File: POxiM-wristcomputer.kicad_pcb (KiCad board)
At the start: 4 copper layers, 40 x 27 mm, 91 parts, among them J1 USB_B_Micro, J14 Jumper_NO_Small, J2 AudioJack4_Ground

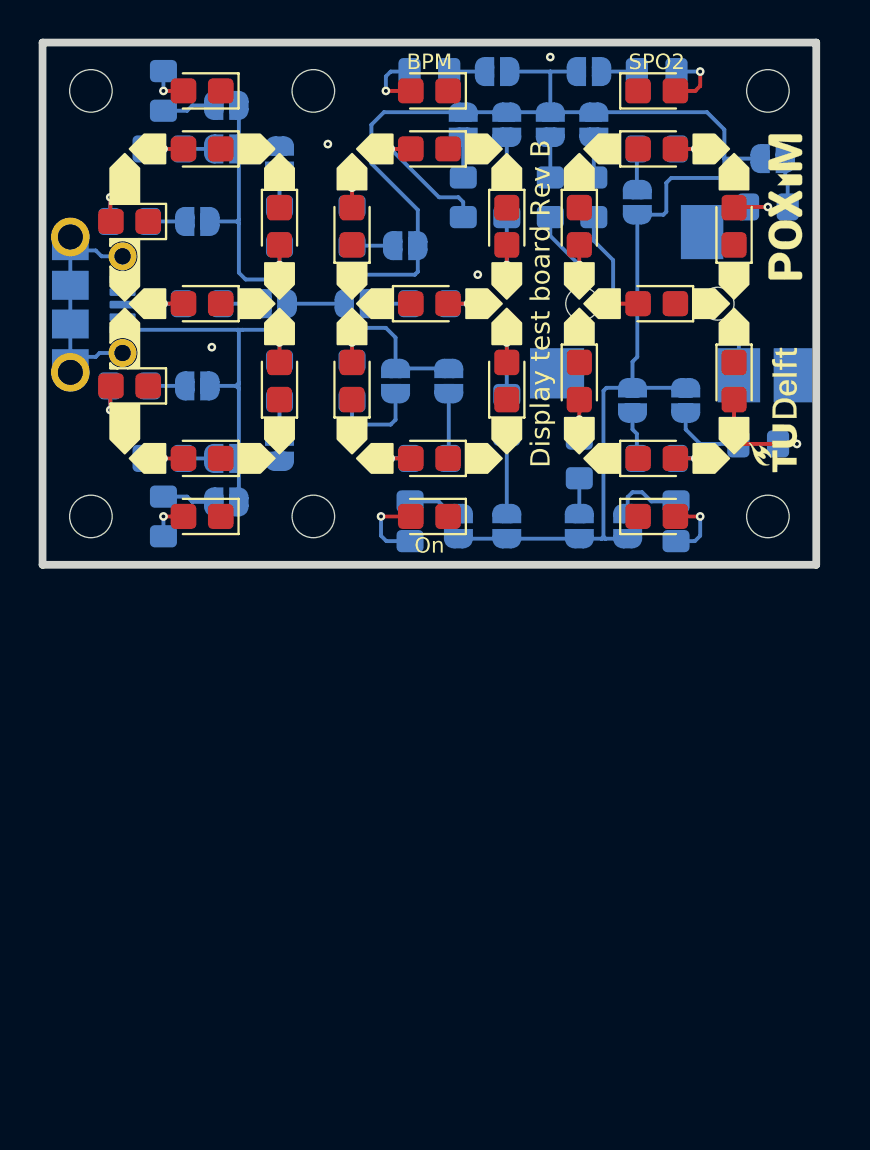
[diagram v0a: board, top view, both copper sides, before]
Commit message: Start reworking sing supply ripple issues.
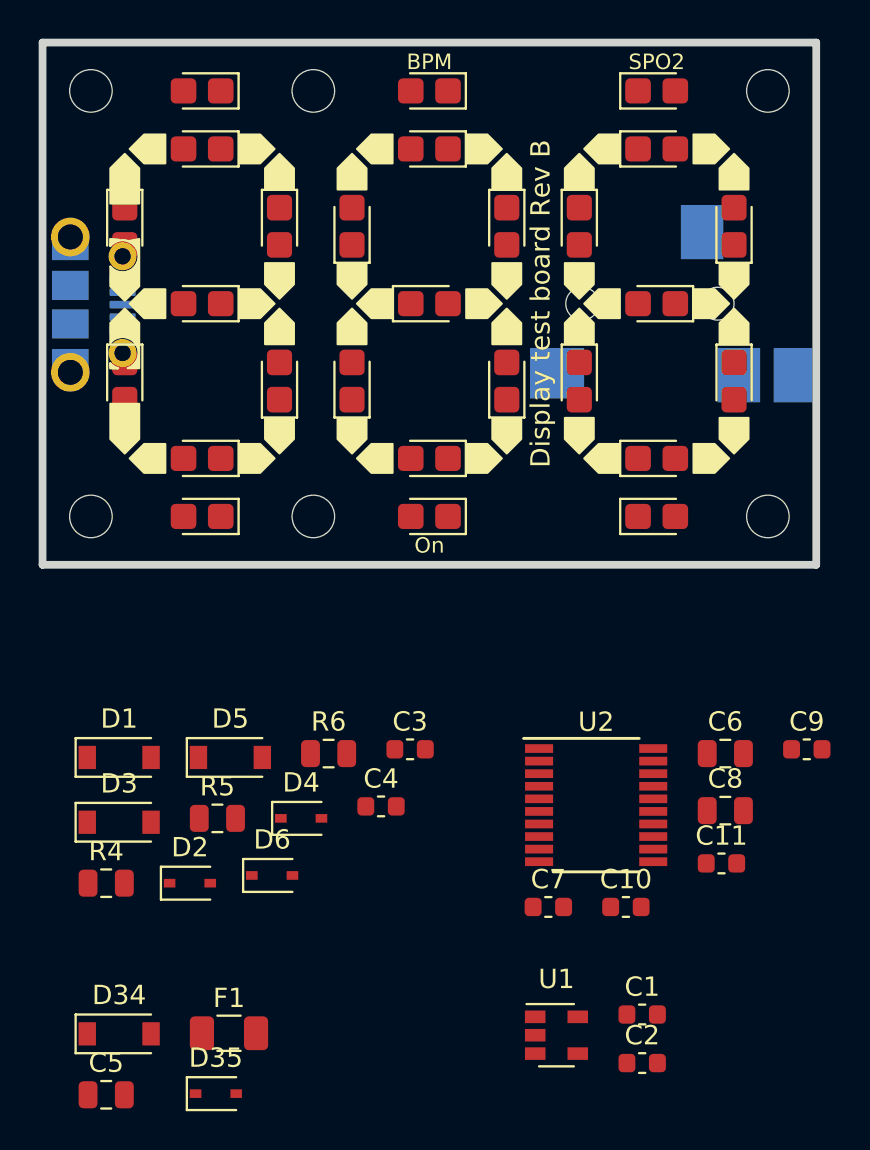
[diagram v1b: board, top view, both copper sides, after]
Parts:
- removed the D10 at (82.2, 127.5)
- removed the D23 at (94.0, 127.5)
- removed the D25 at (94.0, 135.5)
- removed the D28 at (86.0, 135.5)
- removed the D29 at (86.0, 127.5)
- removed G***: LOGO, POxiM-logos:TUDelftLogo_W7_5mm
- removed G***: LOGO, POxiM-logos:POxiMLogo_GoldHeart_W7_5mm
- removed J14, JP1, JP16, JP18, JP2, JP20, JP27, JP28, JP29, JP3, JP30, JP31, JP8: Jumper_NO_Small, POxiM-uncategorised:SolderJumper-2_P1.3mm_Open_RoundedPad1.0x1.5mm
- removed JP10, JP11, JP12, JP13, JP15, JP17, JP19, JP21, JP22, JP23, JP24, JP25, JP26, JP9: Jumper_NC_Small, POxiM-uncategorised:SolderJumper-2_P1.3mm_SolderBridged_RoundedPad1.0x1.5mm
- removed R1, R10, R11, R12, R13, R14, R15, R16, R17, R18, R19, R2, R20, R21, R22, R23, R24, R25, R26, R27, R28, R29, R3, R30, R7, R8, R9: 4.7kΩ, Resistor_SMD:R_0805_2012Metric_Pad1.15x1.40mm_HandSolder
- added C1: 100nF, Capacitor_SMD:C_0603_1608Metric, F.Cu at (101.0, 168.2)
- added C10: 470nF, Capacitor_SMD:C_0603_1608Metric, F.Cu at (100.2, 162.7)
- added C11: 100nF, Capacitor_SMD:C_0603_1608Metric, F.Cu at (105.1, 160.4)
- added C2: 39pF, Capacitor_SMD:C_0603_1608Metric, F.Cu at (101.0, 170.8)
- added C3: 100nF, Capacitor_SMD:C_0603_1608Metric, F.Cu at (89.0, 154.5)
- added C4: 100nF, Capacitor_SMD:C_0603_1608Metric, F.Cu at (87.5, 157.5)
- added C5: 100µF, Capacitor_SMD:C_0805_2012Metric, F.Cu at (73.3, 172.4)
- added C6: 100µF, Capacitor_SMD:C_0805_2012Metric, F.Cu at (105.3, 154.8)
- added C7: 100nF, Capacitor_SMD:C_0603_1608Metric, F.Cu at (96.2, 162.7)
- added C8: 2.2µF, Capacitor_SMD:C_0805_2012Metric, F.Cu at (105.3, 157.7)
- added C9: 100nF, Capacitor_SMD:C_0603_1608Metric, F.Cu at (109.5, 154.5)
- added D1: 5.2V, Diode_SMD:D_SOD-123, F.Cu at (74.0, 155.0)
- added D15: LED, LED_SMD:LED_0805_2012Metric_Castellated, F.Cu at (86.0, 127.5)
- added D16: LED, LED_SMD:LED_0805_2012Metric_Castellated, F.Cu at (94.0, 127.5)
- added D19: LED, LED_SMD:LED_0805_2012Metric_Castellated, F.Cu at (94.0, 135.5)
- added D2: ~, Diode_SMD:D_SOD-323, F.Cu at (77.6, 161.5)
- added D3: 5.2V, Diode_SMD:D_SOD-123, F.Cu at (74.0, 158.3)
- added D34: 5.2V, Diode_SMD:D_SOD-123, F.Cu at (74.0, 169.2)
- added D35: ~, Diode_SMD:D_SOD-323, F.Cu at (79.0, 172.3)
- added D4: ~, Diode_SMD:D_SOD-323, F.Cu at (83.4, 158.1)
- added D5: 5.2V, Diode_SMD:D_SOD-123, F.Cu at (79.7, 155.0)
- added D6: ~, Diode_SMD:D_SOD-323, F.Cu at (81.9, 161.1)
- added D8: LED, LED_SMD:LED_0805_2012Metric_Castellated, F.Cu at (74.2, 127.5)
- added D9: LED, LED_SMD:LED_0805_2012Metric_Castellated, F.Cu at (82.2, 127.5)
- added F1: 100mA, Resistor_SMD:R_1206_3216Metric, F.Cu at (79.6, 169.2)
- added R4: 390Ω, Resistor_SMD:R_0805_2012Metric, F.Cu at (73.3, 161.5)
- added R5: 33kΩ, Resistor_SMD:R_0805_2012Metric, F.Cu at (79.0, 158.1)
- added R6: 33kΩ, Resistor_SMD:R_0805_2012Metric, F.Cu at (84.8, 154.8)
- added U1: LM321, Package_TO_SOT_SMD:SOT-23-5, F.Cu at (96.6, 169.3)
- added U2: STM8S003F3P, Package_SO:TSSOP-20_4.4x6.5mm_P0.65mm, F.Cu at (98.6, 157.4)
- J1: value USB_B_Micro -> Power in
- J2: value AudioJack4_Ground -> To finger probe
- moved D18 14.2 mm to (86.0, 135.5), turned to 90 degrees
- moved D11 0.35 mm to (74.2, 135.5), turned to 270 degrees
- renumbered D20 to D10, D16 to D11, D14 to D13, D21 to D14, D30 to D17, D27 to D20, D1 to D21, D7 to D22, D24 to D23, D17 to D24, D26 to D25, D9 to D26, D2 to D27, D19 to D28, D22 to D29, D15 to D30, D3 to D31, D11 to D32, D13 to D33, D8 to D7
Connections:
- net Net-(J1-Pad2) renamed /USB interface/Data-
- net Net-(J1-Pad3) renamed /USB interface/Data+
- net Net-(J2-PadS) renamed /Signal conditioning/PhotoDiode
- D10 pad 1: GND -> Net-(D10-Pad1)
- D10 pad 2: Net-(D20-Pad2) -> /Display/Segment3i
- D11 pad 1: GND -> Net-(D10-Pad1)
- D11 pad 2: Net-(D16-Pad2) -> /Display/Segment4i
- D12 pad 1: GND -> Net-(D10-Pad1)
- D12 pad 2: Net-(D12-Pad2) -> /Display/Segment5i
- D13 pad 1: GND -> Net-(D10-Pad1)
- D13 pad 2: Net-(D14-Pad2) -> /Display/Segment6i
- D14 pad 1: GND -> Net-(D14-Pad1)
- D14 pad 2: Net-(D21-Pad2) -> /Display/Segment0i
- D17 pad 1: GND -> Net-(D14-Pad1)
- D17 pad 2: Net-(D30-Pad2) -> /Display/Segment3i
- D18 pad 1: GND -> Net-(D14-Pad1)
- D18 pad 2: Net-(D18-Pad2) -> /Display/Segment4i
- D20 pad 1: GND -> Net-(D14-Pad1)
- D20 pad 2: Net-(D27-Pad2) -> /Display/Segment6i
- D21 pad 1: GND -> /Display/Segment0i
- D21 pad 2: Net-(D1-Pad2) -> Net-(D21-Pad2)
- D22 pad 1: GND -> Net-(D22-Pad1)
- D22 pad 2: Net-(D7-Pad2) -> /Display/Segment0i
- D23 pad 1: GND -> /Display/Segment1i
- D23 pad 2: Net-(D24-Pad2) -> Net-(D21-Pad2)
- D24 pad 1: GND -> Net-(D22-Pad1)
- D24 pad 2: Net-(D17-Pad2) -> /Display/Segment1i
- D25 pad 1: GND -> /Display/Segment2i
- D25 pad 2: Net-(D26-Pad2) -> Net-(D21-Pad2)
- D26 pad 1: GND -> Net-(D22-Pad1)
- D26 pad 2: Net-(D9-Pad2) -> /Display/Segment2i
- D27 pad 1: GND -> /Display/Segment3i
- D27 pad 2: Net-(D2-Pad2) -> Net-(D21-Pad2)
- D28 pad 1: GND -> Net-(D22-Pad1)
- D28 pad 2: Net-(D19-Pad2) -> /Display/Segment3i
- D29 pad 1: GND -> /Display/Segment4i
- D29 pad 2: Net-(D22-Pad2) -> Net-(D21-Pad2)
- D30 pad 1: GND -> Net-(D22-Pad1)
- D30 pad 2: Net-(D15-Pad2) -> /Display/Segment4i
- D31 pad 1: GND -> /Display/Segment5i
- D31 pad 2: Net-(D3-Pad2) -> Net-(D21-Pad2)
- D32 pad 1: GND -> Net-(D22-Pad1)
- D32 pad 2: Net-(D11-Pad2) -> /Display/Segment5i
- D33 pad 1: GND -> Net-(D22-Pad1)
- D33 pad 2: Net-(D13-Pad2) -> /Display/Segment6i
- D7 pad 1: GND -> Net-(D10-Pad1)
- D7 pad 2: Net-(D8-Pad2) -> /Display/Segment0i
- J1 pad 1: +5V -> /USB interface/5V_input
- J2 pad R1: Net-(J2-PadR1) -> /Signal conditioning/LEDOut.IR
- J2 pad R2: GND -> +5V
- J2 pad T: Net-(J2-PadT) -> /Signal conditioning/LEDOut.Red
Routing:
- net +5V: track 128.8 -> 0.00 mm
- net GND: track 15.5 -> 0.00 mm, vias 5 -> 0
- net Net-(D21-Pad2): track 6.70 -> 0.00 mm, vias 1 -> 0
- net Net-(D11-Pad2): track 6.22 -> 0.00 mm, vias 1 -> 0
- net Net-(D19-Pad2): track 6.18 -> 0.00 mm, vias 1 -> 0
- net Net-(JP29-Pad2): track 4.78 -> 0.00 mm
- net Net-(D22-Pad2): track 4.15 -> 0.00 mm, vias 1 -> 0
- net Net-(D17-Pad2): track 4.13 -> 0.00 mm, vias 1 -> 0
- net Net-(JP26-Pad2): track 4.07 -> 0.00 mm
- net Net-(JP12-Pad2): track 3.89 -> 0.00 mm
- net Net-(D25-Pad2): track 3.76 -> 0.00 mm, vias 1 -> 0
- net Net-(D3-Pad2): track 3.65 -> 0.00 mm, vias 1 -> 0
- net Net-(JP3-Pad2): track 3.65 -> 0.00 mm
- net Net-(D23-Pad2): track 3.51 -> 0.00 mm, vias 1 -> 0
- net Net-(D26-Pad2): track 3.37 -> 0.00 mm, vias 1 -> 0
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
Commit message: Initial PCB layout
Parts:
- removed C11: 100nF, Capacitor_SMD:C_0603_1608Metric
- added C12: 100nF, POxiM-uncategorised:C_0805_2012Metric_0603_1608Metric, F.Cu at (72.5, 127.0)
- added FID1: Fiducial, Fiducial:Fiducial_0.5mm_Mask1mm, B.Cu at (110.8, 116.2)
- added FID2: Fiducial, Fiducial:Fiducial_0.5mm_Mask1mm, B.Cu at (71.2, 146.8)
- added FID3: Fiducial, Fiducial:Fiducial_0.5mm_Mask1mm, F.Cu at (71.2, 116.2)
- added FID4: Fiducial, Fiducial:Fiducial_0.5mm_Mask1mm, F.Cu at (110.8, 146.8)
- added G***: LOGO, POxiM-logos:POxiMLogo_GoldHeart_W5mm, B.Cu at (84.1, 134.5)
- added JP1: SWIM jumper, POxiM-uncategorised:R_0805_2012Metric_0603_1608Metric, F.Cu at (105.0, 131.0)
- added JP2: UART out jumper, POxiM-uncategorised:R_0805_2012Metric_0603_1608Metric, F.Cu at (105.0, 133.0)
- added Q1: MMBT3904,215, Package_TO_SOT_SMD:SOT-23, F.Cu at (118.0, 106.2)
- added Q2: MMBT3904,215, Package_TO_SOT_SMD:SOT-23, F.Cu at (114.0, 106.2)
- added Q3: MMBT3904,215, Package_TO_SOT_SMD:SOT-23, F.Cu at (110.0, 106.2)
- added Q4: PMBT3906,215, Package_TO_SOT_SMD:SOT-23, F.Cu at (88.0, 102.8)
- added Q5: PMBT3906,215, Package_TO_SOT_SMD:SOT-23, F.Cu at (91.5, 102.7)
- added Q6: PMBT3906,215, Package_TO_SOT_SMD:SOT-23, F.Cu at (95.0, 102.7)
- added Q7: PMBT3906,215, Package_TO_SOT_SMD:SOT-23, F.Cu at (77.8, 153.0)
- added Q8: PMBT3906,215, Package_TO_SOT_SMD:SOT-23, F.Cu at (81.2, 120.8)
- added Q9: PMBT3906,215, Package_TO_SOT_SMD:SOT-23, F.Cu at (76.8, 120.8)
- added R1: 4.7MΩ, POxiM-uncategorised:R_0805_2012Metric_0603_1608Metric, F.Cu at (81.2, 152.2)
- added R10: 560Ω, POxiM-uncategorised:R_0805_2012Metric_0603_1608Metric, F.Cu at (128.0, 115.2)
- added R11: 2.2kΩ, POxiM-uncategorised:R_0805_2012Metric_0603_1608Metric, F.Cu at (78.2, 117.0)
- added R12: 560Ω, POxiM-uncategorised:R_0805_2012Metric_0603_1608Metric, F.Cu at (120.0, 115.2)
- added R13: 3.3kΩ, POxiM-uncategorised:R_0805_2012Metric_0603_1608Metric, F.Cu at (80.2, 117.0)
- added R14: 3.3kΩ, POxiM-uncategorised:R_0805_2012Metric_0603_1608Metric, F.Cu at (119.0, 109.8)
- added R15: 3.3kΩ, POxiM-uncategorised:R_0805_2012Metric_0603_1608Metric, F.Cu at (115.0, 109.8)
- added R16: 3.3kΩ, POxiM-uncategorised:R_0805_2012Metric_0603_1608Metric, F.Cu at (111.0, 109.8)
- added R17: 3.3kΩ, POxiM-uncategorised:R_0805_2012Metric_0603_1608Metric, F.Cu at (87.0, 99.0)
- added R18: 3.3kΩ, POxiM-uncategorised:R_0805_2012Metric_0603_1608Metric, F.Cu at (92.0, 99.0)
- added R19: 3.3kΩ, POxiM-uncategorised:R_0805_2012Metric_0603_1608Metric, F.Cu at (96.0, 99.0)
- added R2: 33kΩ, POxiM-uncategorised:R_0805_2012Metric_0603_1608Metric, F.Cu at (71.2, 138.8)
- added R20: 2.2kΩ, POxiM-uncategorised:R_0805_2012Metric_0603_1608Metric, F.Cu at (72.5, 123.0)
- added R21: 3.3kΩ, POxiM-uncategorised:R_0805_2012Metric_0603_1608Metric, F.Cu at (72.5, 121.0)
- added R22: 68Ω, POxiM-uncategorised:R_0805_2012Metric_0603_1608Metric, F.Cu at (82.2, 117.0)
- added R23: 68Ω, POxiM-uncategorised:R_0805_2012Metric_0603_1608Metric, F.Cu at (76.2, 117.0)
- added R24: 33kΩ, POxiM-uncategorised:R_0805_2012Metric_0603_1608Metric, F.Cu at (81.8, 124.0)
- added R25: 33kΩ, POxiM-uncategorised:R_0805_2012Metric_0603_1608Metric, F.Cu at (72.5, 125.0)
- added R3: 100kΩ, POxiM-uncategorised:R_0805_2012Metric_0603_1608Metric, F.Cu at (77.8, 155.8)
- added R7: 560Ω, POxiM-uncategorised:R_0805_2012Metric_0603_1608Metric, F.Cu at (122.0, 115.2)
- added R8: 560Ω, POxiM-uncategorised:R_0805_2012Metric_0603_1608Metric, F.Cu at (130.0, 115.2)
- added R9: 560Ω, POxiM-uncategorised:R_0805_2012Metric_0603_1608Metric, F.Cu at (124.0, 115.2)
- added TP1: 5V in, TestPoint:TestPoint_THTPad_D1.0mm_Drill0.5mm, F.Cu at (114.4, 127.0)
- added TP2: SWIM, TestPoint:TestPoint_THTPad_D1.0mm_Drill0.5mm, F.Cu at (103.5, 129.2)
- added TP3: UART.TX, TestPoint:TestPoint_THTPad_D1.0mm_Drill0.5mm, F.Cu at (102.5, 133.8)
- added TP4: GND, TestPoint:TestPoint_THTPad_D1.0mm_Drill0.5mm, F.Cu at (114.5, 124.0)
- added TP5: PhotoDiode, TestPoint:TestPoint_THTPad_D1.0mm_Drill0.5mm, F.Cu at (61.6, 139.2)
- added TP6: LED.Red, TestPoint:TestPoint_THTPad_D1.0mm_Drill0.5mm, F.Cu at (57.8, 128.5)
- added TP7: GND, TestPoint:TestPoint_THTPad_D1.0mm_Drill0.5mm, F.Cu at (65.0, 138.8)
- added TP8: LED.IR, TestPoint:TestPoint_THTPad_D1.0mm_Drill0.5mm, F.Cu at (61.3, 129.0)
- added U3: MIC5504-3.3YM5, Package_TO_SOT_SMD:SOT-23-5, F.Cu at (107.0, 138.2)
- C1, C10, C2, C3, C7, C9: footprint Capacitor_SMD:C_0603_1608Metric -> POxiM-uncategorised:C_0805_2012Metric_0603_1608Metric
- C4: value 100nF -> 2.2µF; footprint Capacitor_SMD:C_0603_1608Metric -> POxiM-uncategorised:C_0805_2012Metric_0603_1608Metric
- C5: value 100µF -> 2.2µF; footprint Capacitor_SMD:C_0805_2012Metric -> POxiM-uncategorised:C_0805_2012Metric_0603_1608Metric
- C6: value 100µF -> 100nF; footprint Capacitor_SMD:C_0805_2012Metric -> POxiM-uncategorised:C_0805_2012Metric_0603_1608Metric
- C8: footprint Capacitor_SMD:C_0805_2012Metric -> POxiM-uncategorised:C_0805_2012Metric_0603_1608Metric
- D1, D3, D5: value 5.2V -> Schottky; footprint Diode_SMD:D_SOD-123 -> Diode_SMD:D_SOD-323
- D10, D11, D12, D13, D14, D15, D16, D17, D18, D19, D20, D21, D22, D23, D24, D25, D26, D27, D28, D29, D30, D31, D32, D33, D7, D8, D9: footprint LED_SMD:LED_0805_2012Metric_Castellated -> POxiM-uncategorised:LED_0805_2012Metric_0603_1608Metric; moved to B.Cu
- D2, D35, D4, D6: value ~ -> Schottky
- D34: value 5.2V -> 6.8V
- F1: value 100mA -> 500mA; footprint Resistor_SMD:R_1206_3216Metric -> Resistor_SMD:R_1812_4532Metric
- H1, H2, H3, H4: footprint MountingHole:MountingHole_2.2mm_M2_DIN965 -> POxiM-uncategorised:MountingHole_2.2mm_M2; moved to B.Cu
- H5, H6: footprint MountingHole:MountingHole_2.2mm_M2_DIN965 -> POxiM-uncategorised:AlignmentHole_2.2mm_M2; moved to B.Cu
- J1: footprint POxiM-uncategorised:Micro-B_Molex_105017-0001 -> POxiM-uncategorised:USB_Micro-B_Amphenol_10103594-0001LF_Horizontal; moved to F.Cu
- J2: moved to F.Cu
- R4: value 390Ω -> 100kΩ; footprint Resistor_SMD:R_0805_2012Metric -> POxiM-uncategorised:R_0805_2012Metric_0603_1608Metric
- R5, R6: value 33kΩ -> 560Ω; footprint Resistor_SMD:R_0805_2012Metric -> POxiM-uncategorised:R_0805_2012Metric_0603_1608Metric
- moved R5 68.1 mm to (132.0, 115.2), turned to 270 degrees
- moved D35 59.9 mm to (106.2, 119.0), turned to 90 degrees
- moved D34 58.2 mm to (108.0, 122.0)
- moved R6 57.1 mm to (126.0, 115.2), turned to 270 degrees
- moved C3 55.8 mm to (94.0, 99.0), turned to 90 degrees
- moved F1 52.6 mm to (108.5, 125.2)
- moved C5 45.9 mm to (104.0, 138.2), turned to 90 degrees
- moved J1 42.0 mm to (112.0, 131.5)
- moved C1 38.9 mm to (79.2, 136.0), turned to 180 degrees
- moved H1 37.1 mm to (109.5, 117.5), turned to 180 degrees
- moved H4 37.1 mm to (109.5, 145.5), turned to 180 degrees
- moved C6 36.8 mm to (81.8, 126.5)
- moved C2 36.5 mm to (79.2, 141.5), turned to 180 degrees
- moved U1 35.1 mm to (79.2, 138.8)
- moved H2 35.1 mm to (72.5, 117.5), turned to 180 degrees
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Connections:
- C1 pad 1: +5V -> +3V3
- C3 pad 1: /Signal conditioning/LEDOut.IR -> Net-(C3-Pad1)
- C4 pad 1: /Signal conditioning/LEDOut.Red -> +5V
- C5 pad 1: +5V -> +3V3
- C6 pad 1: Net-(C11-Pad1) -> /Signal conditioning/LEDOut.Red
- C8 pad 1: Net-(C11-Pad1) -> +3V3
- C9 pad 1: Net-(C11-Pad1) -> +3V3
- D1 pad 1: /Microcontroller/LED.IR -> /Microcontroller/LED.Red
- D1 pad 2: GND -> Net-(D1-Pad2)
- D10 pad 2: /Display/Segment3i -> /Display/Segment3
- D11 pad 2: /Display/Segment4i -> /Display/Segment4
- D12 pad 2: /Display/Segment5i -> /Display/Segment5
- D13 pad 2: /Display/Segment6i -> /Display/Segment6
- D14 pad 2: /Display/Segment0i -> /Display/Segment0
- D15 pad 2: /Display/Segment1i -> /Display/Segment1
- D16 pad 2: /Display/Segment2i -> /Display/Segment2
- D17 pad 2: /Display/Segment3i -> /Display/Segment3
- D18 pad 2: /Display/Segment4i -> /Display/Segment4
- D19 pad 2: /Display/Segment5i -> /Display/Segment5
- D2 pad 2: GND -> Net-(D2-Pad2)
- D20 pad 2: /Display/Segment6i -> /Display/Segment6
- D21 pad 1: /Display/Segment0i -> /Display/Segment0
- D22 pad 2: /Display/Segment0i -> /Display/Segment0
- D23 pad 1: /Display/Segment1i -> /Display/Segment1
- D24 pad 2: /Display/Segment1i -> /Display/Segment1
- D25 pad 1: /Display/Segment2i -> /Display/Segment2
- D26 pad 2: /Display/Segment2i -> /Display/Segment2
- D27 pad 1: /Display/Segment3i -> /Display/Segment6
- D28 pad 2: /Display/Segment3i -> /Display/Segment3
- D29 pad 1: /Display/Segment4i -> /Display/Segment4
- D3 pad 1: /Microcontroller/LED.Red -> /Signal conditioning/LEDOut.Red
- D3 pad 2: GND -> Net-(D1-Pad2)
- D30 pad 2: /Display/Segment4i -> /Display/Segment4
- D31 pad 1: /Display/Segment5i -> /Display/Segment5
- D32 pad 2: /Display/Segment5i -> /Display/Segment5
- D33 pad 2: /Display/Segment6i -> /Display/Segment6
- D4 pad 1: /Microcontroller/LED.Red -> /Signal conditioning/LEDOut.IR
- D4 pad 2: GND -> Net-(D2-Pad2)
- D5 pad 1: /Signal conditioning/PhotoDiodeInternal -> GND
- D5 pad 2: GND -> /Signal conditioning/PhotoDiodeInternal
- D7 pad 2: /Display/Segment0i -> /Display/Segment0
- D8 pad 2: /Display/Segment1i -> /Display/Segment1
- D9 pad 2: /Display/Segment2i -> /Display/Segment2
- J2 pad R2: +5V -> GND
- R4 pad 1: /Signal conditioning/LEDOut.IR -> Net-(Q7-Pad3)
- R4 pad 2: /Microcontroller/LED.IR -> GND
- R5 pad 1: GND -> +5V
- R5 pad 2: /Signal conditioning/LEDOut.IR -> /Display/Segment1
- R6 pad 1: GND -> +5V
- R6 pad 2: /Signal conditioning/LEDOut.Red -> /Display/Segment2
- U1 pad 1: +5V -> GND
- U1 pad 5: +5V -> +3V3
- U2 pad 10: /Display/Segment2 -> /Display/Common2
- U2 pad 13: /Microcontroller/LED.IR -> /Microcontroller/LED.Red
- U2 pad 14: /Microcontroller/LED.Red -> /Microcontroller/LED.IR
- U2 pad 17: /Display/Common2 -> /Display/Segment0
- U2 pad 19: /Display/Common0 -> /Display/Segment1
- U2 pad 20: /Display/Common1 -> /Display/Segment2
- U2 pad 5: /Display/Segment0 -> /Display/Common0
- U2 pad 6: /Display/Segment1 -> /Display/Common1
- U2 pad 9: Net-(C11-Pad1) -> +3V3
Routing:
- net Net-(D21-Pad2): track 0.00 -> 102.0 mm
- net Net-(D22-Pad1): track 0.00 -> 88.8 mm
- net /Display/Segment4: track 0.00 -> 57.9 mm
- net /Display/Segment1: track 0.00 -> 51.8 mm
- net /Display/Segment5: track 0.00 -> 51.5 mm
- net /Display/Segment2: track 0.00 -> 49.2 mm
- net Net-(D14-Pad1): track 0.00 -> 46.1 mm, vias 0 -> 4
- net Net-(D10-Pad1): track 0.00 -> 43.9 mm
- net /Display/Segment6: track 0.00 -> 41.6 mm
- net /Display/Segment0: track 0.00 -> 40.0 mm
- net /Display/Segment3: track 0.00 -> 38.2 mm
- net +5V: track 0.00 -> 31.6 mm, vias 0 -> 2
- net /Microcontroller/ADC.input: track 0.00 -> 17.4 mm
- net /Signal conditioning/LEDOut.Red: track 0.00 -> 15.3 mm
- net /Microcontroller/ADC.feedback: track 0.00 -> 14.4 mm
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- added copper zone on In1.Cu, net GND
- added copper zone on In2.Cu, net GND
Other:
- board size 40 x 27 mm -> 42 x 33 mm
- board text added: "Rev A"
- board text removed: "Display test board Rev B"

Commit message: Finalise wrist computer rev A
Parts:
- removed the G*** at (84.1, 134.5)
- added C11: 100nF, POxiM-uncategorised:C_0805_2012Metric_0603_1608Metric, F.Cu at (105.8, 129.0)
- added D36: Schottky, POxiM-uncategorised:D_SOD-323, F.Cu at (106.2, 138.2)
- added D37: Schottky, POxiM-uncategorised:D_SOD-323, F.Cu at (102.8, 138.2)
- added D38: Schottky, POxiM-uncategorised:D_SOD-323, F.Cu at (106.2, 140.8)
- added D39: Schottky, POxiM-uncategorised:D_SOD-323, F.Cu at (102.8, 140.8)
- added D40: 5.6V, POxiM-uncategorised:D_SOD-123, F.Cu at (109.8, 139.0)
- added G***: LOGO, POxiM-logos:TUDelftLogo_W10mm, B.Cu at (96.2, 142.2)
- added G***: LOGO, POxiM-logos:POxiMLogo_GoldHeart_W10mm, B.Cu at (82.8, 142.8)
- added G***: LOGO, POxiM-logos:POxiMLogo_W7_5mm, F.Cu at (92.0, 134.2)
- added NT1: Net-Tie_2, NetTie:NetTie-2_SMD_Pad0.5mm, F.Cu at (102.5, 145.5)
- added NT2: Net-Tie_2, NetTie:NetTie-2_SMD_Pad0.5mm, F.Cu at (102.5, 144.5)
- added TP9: 3.3V, POxiM-uncategorised:TestPoint_THTPad_D1.0mm_Drill0.5mm, F.Cu at (86.5, 140.2)
- C12, C6: value 100nF -> 2.2µF
- D1, D2, D3, D35, D4, D5, D6: footprint Diode_SMD:D_SOD-323 -> POxiM-uncategorised:D_SOD-323
- D34: footprint Diode_SMD:D_SOD-123 -> POxiM-uncategorised:D_SOD-123
- FID1, FID2, FID3, FID4: footprint Fiducial:Fiducial_0.5mm_Mask1mm -> POxiM-uncategorised:Fiducial_1mm_Mask2mm
- H1, H2, H3, H4: footprint POxiM-uncategorised:MountingHole_2.2mm_M2 -> MountingHole:MountingHole_2.2mm_M2
- TP1, TP2, TP3, TP4, TP5, TP6, TP8: footprint TestPoint:TestPoint_THTPad_D1.0mm_Drill0.5mm -> POxiM-uncategorised:TestPoint_THTPad_D1.0mm_Drill0.5mm
- TP7: value GND -> GNDA; footprint TestPoint:TestPoint_THTPad_D1.0mm_Drill0.5mm -> POxiM-uncategorised:TestPoint_THTPad_D1.0mm_Drill0.5mm
- moved R5 41.2 mm to (93.0, 128.5)
- moved R6 40.1 mm to (89.8, 132.5), turned to 180 degrees
- moved R8 34.6 mm to (98.0, 128.5)
- moved R10 34.3 mm to (98.5, 132.8), turned to 180 degrees
- moved R12 33.7 mm to (89.8, 130.0), turned to 180 degrees
- moved Q1 30.7 mm to (91.2, 121.2), turned to 270 degrees
- moved R7 29.6 mm to (95.5, 128.5)
- moved R17 28.7 mm to (99.2, 125.0), turned to 180 degrees
- moved Q4 28.4 mm to (103.2, 126.8)
- moved FID3 27.7 mm to (74.2, 143.8)
- moved FID4 27.5 mm to (108.0, 119.4)
- moved R9 27.0 mm to (100.5, 128.5)
- moved R14 27.0 mm to (95.2, 122.5), turned to 0 degrees
- moved Q3 26.5 mm to (91.2, 125.0), turned to 270 degrees
- moved TP6 26.3 mm to (84.0, 127.5), turned to 0 degrees
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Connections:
- C1 pad 2: GND -> GNDREF
- C12 pad 2: GND -> GNDA
- C6 pad 2: GND -> GNDA
- D5 pad 1: GND -> GNDA
- D6 pad 2: GND -> GNDA
- J2 pad R2: GND -> GNDA
- Q2 pad 3: Net-(D14-Pad1) -> Net-(D22-Pad1)
- Q3 pad 3: Net-(D22-Pad1) -> Net-(D14-Pad1)
- R13 pad 1: GND -> GNDA
- R15 pad 2: /Display/Common1 -> /Display/Common2
- R16 pad 2: /Display/Common2 -> /Display/Common1
- R17 pad 2: /Display/Common0 -> /Display/Common1
- R18 pad 2: /Display/Common1 -> /Display/Common0
- R21 pad 1: GND -> GNDA
- R4 pad 2: GND -> GNDREF
- TP7 pad 1: GND -> GNDA
- U1 pad 1: GND -> GNDREF
- U1 pad 2: GND -> GNDREF
- U2 pad 11: /Display/Segment4 -> /Display/Segment6
- U2 pad 12: /Display/Segment3 -> /Display/Segment5
- U2 pad 13: /Microcontroller/LED.Red -> /Microcontroller/LED.IR
- U2 pad 14: /Microcontroller/LED.IR -> /Microcontroller/LED.Red
- U2 pad 15: /Display/Segment5 -> /Display/Segment4
- U2 pad 16: /Display/Segment6 -> /Display/Segment3
- U2 pad 17: /Display/Segment0 -> /Display/Segment1
- U2 pad 19: /Display/Segment1 -> /Display/Segment0
- U2 pad 5: /Display/Common0 -> /Display/Common1
- U2 pad 6: /Display/Common1 -> /Display/Common0
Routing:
- net +3V3: track 12.4 -> 121.5 mm, vias 0 -> 3
- net +5V: track 31.6 -> 73.4 mm, vias 2 -> 3
- net GND: track 4.86 -> 31.7 mm, vias 20 -> 134
- net /Display/Common0: track 11.7 -> 32.9 mm, vias 0 -> 2
- net /Display/Common1: track 11.7 -> 32.3 mm, vias 0 -> 2
- net /Display/Common2: track 10.4 -> 30.7 mm, vias 0 -> 2
- net GNDA: track 0.00 -> 18.0 mm, vias 0 -> 7
- net Net-(D10-Pad1): track 43.9 -> 61.7 mm, vias 0 -> 1
- net /USB interface/DataTX: track 11.2 -> 28.3 mm, vias 1 -> 3
- net /Microcontroller/SWIM: track 11.8 -> 27.8 mm, vias 1 -> 2
- net /Microcontroller/LED.IR: track 11.4 -> 24.8 mm
- net /Display/Segment0: track 40.0 -> 53.1 mm, vias 0 -> 1
- net /Display/Segment6: track 41.6 -> 53.8 mm, vias 0 -> 1
- net /Microcontroller/LED.Red: track 11.4 -> 23.0 mm
- net GNDREF: track 0.00 -> 11.6 mm, vias 0 -> 4
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- added copper zone on In1.Cu, net GNDA
- added copper zone on In1.Cu, net GNDREF
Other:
- net class Default: clearance 0.1 -> 0.2; trace_width 0.1 -> 0.2
- rule trace_clearance: 0.1 -> 0.2
- rule trace_min: 0.1 -> 0.2
- board text added: "3.3V"
- board text added: "5V"
- board text added: "GND"
- board text added: "GNDA"
- board text added: "IR"
- board text added: "PD"
- board text added: "Red"
- board text added: "SWIM"
- board text added: "UART.TX"
- board text added: "Wrist computer Rev A"
- board text removed: "Rev A"
